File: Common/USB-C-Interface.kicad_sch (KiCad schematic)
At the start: 6 parts

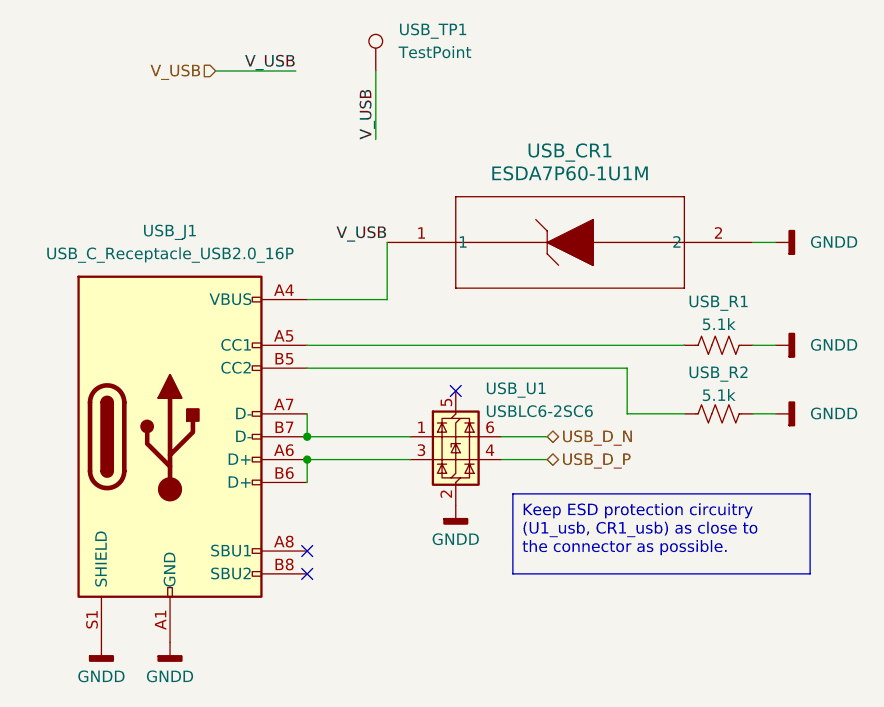
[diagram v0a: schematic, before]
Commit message: Renamed GPS Module PCB files to Radio Module
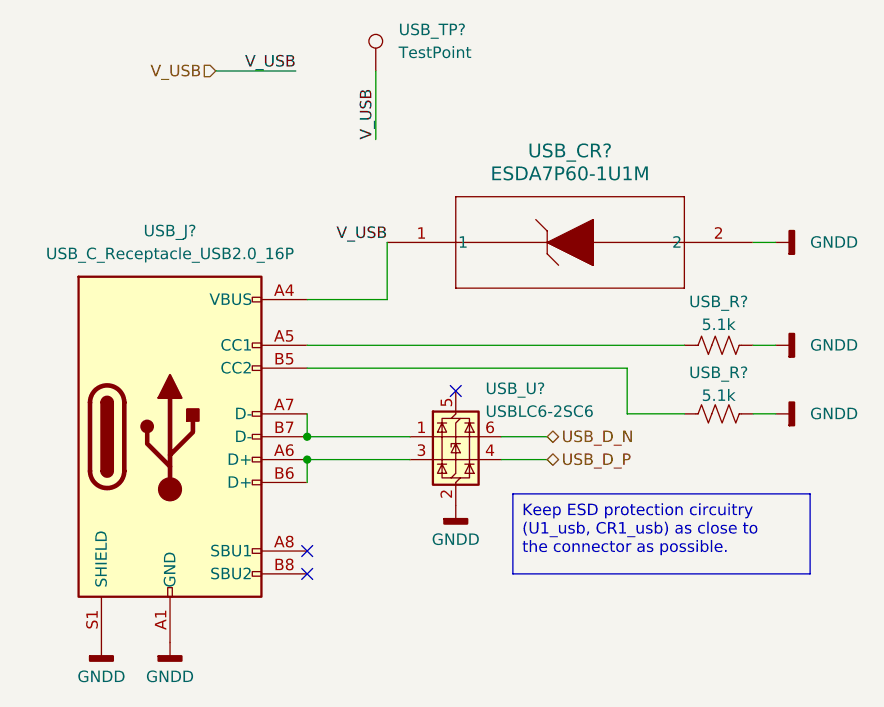
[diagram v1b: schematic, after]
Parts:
- renumbered USB_CR1 to USB_CR?, USB_J1 to USB_J?, USB_R2 to USB_R?, USB_R1 to USB_R?, USB_TP1 to USB_TP?, USB_U1 to USB_U?
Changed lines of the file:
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@@
 		(on_board yes)
 		(dnp no)
-		(property "Reference" "USB_U1"
+		(property "Reference" "USB_U?"
 			(at 82.042 72.136 0)
 			(effects
@@
 		)
 		(instances
+			(project "Radio-Module"
+				(path "/acc63f22-7eb8-450a-9af4-da5f4b8157d9/066db7ca-fd8b-46d1-a06b-412eb11482f3"
+					(reference "USB_U?")
+					(unit 1)
+				)
+			)
 			(project "Main-Module"
 				(path "/c41b490b-5ab6-4438-aea0-388670bb08f4/b23d16a1-3c5b-4321-8b30-5d6992e2f62d"
@@
 		(dnp no)
 		(fields_autoplaced yes)
-		(property "Reference" "USB_J1"
+		(property "Reference" "USB_J?"
 			(at 46.99 54.61 0)
 			(effects
@@
 		)
 		(instances
+			(project "Radio-Module"
+				(path "/acc63f22-7eb8-450a-9af4-da5f4b8157d9/066db7ca-fd8b-46d1-a06b-412eb11482f3"
+					(reference "USB_J?")
+					(unit 1)
+				)
+			)
 			(project "Main-Module"
 				(path "/c41b490b-5ab6-4438-aea0-388670bb08f4/b23d16a1-3c5b-4321-8b30-5d6992e2f62d"
@@
 		(dnp no)
 		(fields_autoplaced yes)
-		(property "Reference" "#PWR037"
+		(property "Reference" "#PWR?"
 			(at 46.99 106.68 0)
 			(effects
@@
 		)
 		(instances
+			(project "Radio-Module"
+				(path "/acc63f22-7eb8-450a-9af4-da5f4b8157d9/066db7ca-fd8b-46d1-a06b-412eb11482f3"
+					(reference "#PWR?")
+					(unit 1)
+				)
+			)
 			(project "Main-Module"
 				(path "/c41b490b-5ab6-4438-aea0-388670bb08f4/b23d16a1-3c5b-4321-8b30-5d6992e2f62d"
@@
 		(dnp no)
 		(fields_autoplaced yes)
-		(property "Reference" "#PWR039"
+		(property "Reference" "#PWR?"
 			(at 120.65 55.88 0)
 			(effects
@@
 		)
 		(instances
+			(project "Radio-Module"
+				(path "/acc63f22-7eb8-450a-9af4-da5f4b8157d9/066db7ca-fd8b-46d1-a06b-412eb11482f3"
+					(reference "#PWR?")
+					(unit 1)
+				)
+			)
 			(project "Main-Module"
 				(path "/c41b490b-5ab6-4438-aea0-388670bb08f4/b23d16a1-3c5b-4321-8b30-5d6992e2f62d"
@@
 		(dnp no)
 		(fields_autoplaced yes)
-		(property "Reference" "#PWR036"
+		(property "Reference" "#PWR?"
 			(at 39.37 106.68 0)
 			(effects
@@
 		)
 		(instances
+			(project "Radio-Module"
+				(path "/acc63f22-7eb8-450a-9af4-da5f4b8157d9/066db7ca-fd8b-46d1-a06b-412eb11482f3"
+					(reference "#PWR?")
+					(unit 1)
+				)
+			)
 			(project "Main-Module"
 				(path "/c41b490b-5ab6-4438-aea0-388670bb08f4/b23d16a1-3c5b-4321-8b30-5d6992e2f62d"
@@
 		(on_board yes)
 		(dnp no)
-		(property "Reference" "USB_R2"
+		(property "Reference" "USB_R?"
 			(at 107.95 70.358 90)
 			(effects
@@
 		)
 		(instances
+			(project "Radio-Module"
+				(path "/acc63f22-7eb8-450a-9af4-da5f4b8157d9/066db7ca-fd8b-46d1-a06b-412eb11482f3"
+					(reference "USB_R?")
+					(unit 1)
+				)
+			)
 			(project "Main-Module"
 				(path "/c41b490b-5ab6-4438-aea0-388670bb08f4/b23d16a1-3c5b-4321-8b30-5d6992e2f62d"
@@
 		(on_board yes)
 		(dnp no)
-		(property "Reference" "USB_R1"
+		(property "Reference" "USB_R?"
 			(at 107.95 62.484 90)
 			(effects
@@
 		)
 		(instances
+			(project "Radio-Module"
+				(path "/acc63f22-7eb8-450a-9af4-da5f4b8157d9/066db7ca-fd8b-46d1-a06b-412eb11482f3"
+					(reference "USB_R?")
+					(unit 1)
+				)
+			)
 			(project "Main-Module"
 				(path "/c41b490b-5ab6-4438-aea0-388670bb08f4/b23d16a1-3c5b-4321-8b30-5d6992e2f62d"
@@
 		(dnp no)
 		(fields_autoplaced yes)
-		(property "Reference" "USB_CR1"
+		(property "Reference" "USB_CR?"
 			(at 91.44 45.72 0)
 			(effects
@@
 		)
 		(instances
+			(project "Radio-Module"
+				(path "/acc63f22-7eb8-450a-9af4-da5f4b8157d9/066db7ca-fd8b-46d1-a06b-412eb11482f3"
+					(reference "USB_CR?")
+					(unit 1)
+				)
+			)
 			(project "Main-Module"
 				(path "/c41b490b-5ab6-4438-aea0-388670bb08f4/b23d16a1-3c5b-4321-8b30-5d6992e2f62d"
@@
 		(dnp no)
 		(fields_autoplaced yes)
-		(property "Reference" "#PWR041"
+		(property "Reference" "#PWR?"
 			(at 120.65 74.93 0)
 			(effects
@@
 		)
 		(instances
+			(project "Radio-Module"
+				(path "/acc63f22-7eb8-450a-9af4-da5f4b8157d9/066db7ca-fd8b-46d1-a06b-412eb11482f3"
+					(reference "#PWR?")
+					(unit 1)
+				)
+			)
 			(project "Main-Module"
 				(path "/c41b490b-5ab6-4438-aea0-388670bb08f4/b23d16a1-3c5b-4321-8b30-5d6992e2f62d"
@@
 		(dnp no)
 		(fields_autoplaced yes)
-		(property "Reference" "#PWR038"
+		(property "Reference" "#PWR?"
 			(at 78.74 91.44 0)
 			(effects
@@
 		)
 		(instances
+			(project "Radio-Module"
+				(path "/acc63f22-7eb8-450a-9af4-da5f4b8157d9/066db7ca-fd8b-46d1-a06b-412eb11482f3"
+					(reference "#PWR?")
+					(unit 1)
+				)
+			)
 			(project "Main-Module"
 				(path "/c41b490b-5ab6-4438-aea0-388670bb08f4/b23d16a1-3c5b-4321-8b30-5d6992e2f62d"
@@
 		(dnp no)
 		(fields_autoplaced yes)
-		(property "Reference" "#PWR040"
+		(property "Reference" "#PWR?"
 			(at 120.65 67.31 0)
 			(effects
@@
 		)
 		(instances
+			(project "Radio-Module"
+				(path "/acc63f22-7eb8-450a-9af4-da5f4b8157d9/066db7ca-fd8b-46d1-a06b-412eb11482f3"
+					(reference "#PWR?")
+					(unit 1)
+				)
+			)
 			(project "Main-Module"
 				(path "/c41b490b-5ab6-4438-aea0-388670bb08f4/b23d16a1-3c5b-4321-8b30-5d6992e2f62d"
@@
 		(dnp no)
 		(fields_autoplaced yes)
-		(property "Reference" "USB_TP1"
+		(property "Reference" "USB_TP?"
 			(at 72.39 32.2579 0)
 			(effects
@@
 		)
 		(instances
-			(project "Main-Module"
-				(path "/c41b490b-5ab6-4438-aea0-388670bb08f4/b23d16a1-3c5b-4321-8b30-5d6992e2f62d"
+			(project "Radio-Module"
+				(path "/acc63f22-7eb8-450a-9af4-da5f4b8157d9/066db7ca-fd8b-46d1-a06b-412eb11482f3"
+					(reference "USB_TP?")
+					(unit 1)
+				)
+			)
+			(project "Main-Module"
+				(path "/c41b490b-5ab6-4438-aea0-388670bb08f4/b23d16a1-3c5b-4321-8b30-5d6992e2f62d"

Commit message: Schematic for STM32U545RE
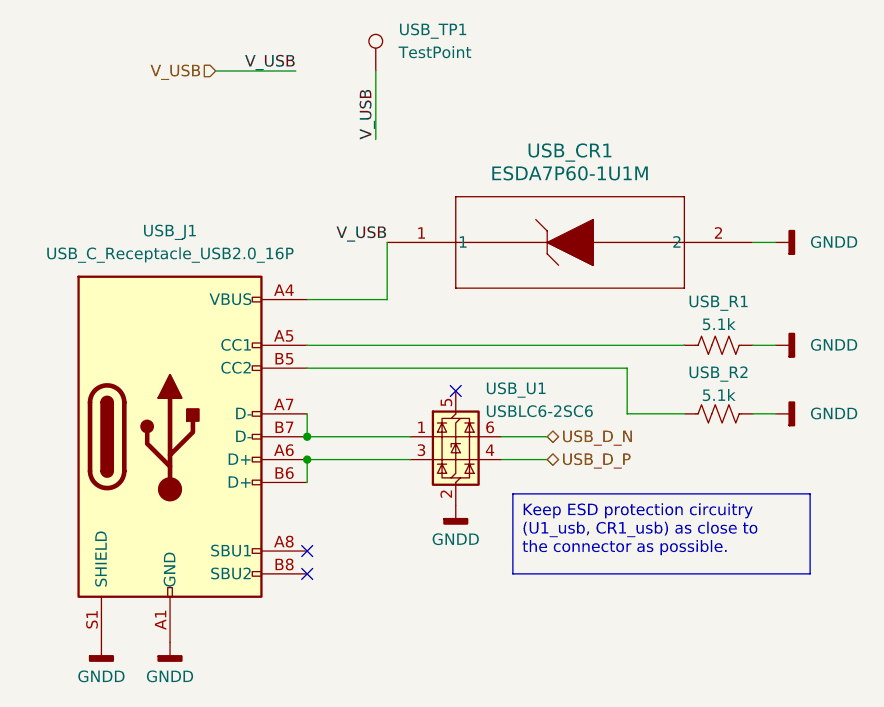
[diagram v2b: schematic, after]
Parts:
- gave numbers to parts that had none: 6
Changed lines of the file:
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@@
 		(on_board yes)
 		(dnp no)
-		(property "Reference" "USB_U?"
+		(property "Reference" "USB_U1"
 			(at 82.042 72.136 0)
 			(effects
@@
 		)
 		(instances
+			(project "USB-C-Interface"
+				(path "/7c253a73-a3ad-4431-8c8c-7421e0c0a047"
+					(reference "USB_U1")
+					(unit 1)
+				)
+			)
 			(project "Radio-Module"
 				(path "/acc63f22-7eb8-450a-9af4-da5f4b8157d9/066db7ca-fd8b-46d1-a06b-412eb11482f3"
@@
 		(dnp no)
 		(fields_autoplaced yes)
-		(property "Reference" "USB_J?"
+		(property "Reference" "USB_J1"
 			(at 46.99 54.61 0)
 			(effects
@@
 		)
 		(instances
+			(project "USB-C-Interface"
+				(path "/7c253a73-a3ad-4431-8c8c-7421e0c0a047"
+					(reference "USB_J1")
+					(unit 1)
+				)
+			)
 			(project "Radio-Module"
 				(path "/acc63f22-7eb8-450a-9af4-da5f4b8157d9/066db7ca-fd8b-46d1-a06b-412eb11482f3"
@@
 		(dnp no)
 		(fields_autoplaced yes)
-		(property "Reference" "#PWR?"
+		(property "Reference" "#PWR02"
 			(at 46.99 106.68 0)
 			(effects
@@
 		)
 		(instances
+			(project "USB-C-Interface"
+				(path "/7c253a73-a3ad-4431-8c8c-7421e0c0a047"
+					(reference "#PWR02")
+					(unit 1)
+				)
+			)
 			(project "Radio-Module"
 				(path "/acc63f22-7eb8-450a-9af4-da5f4b8157d9/066db7ca-fd8b-46d1-a06b-412eb11482f3"
@@
 		(dnp no)
 		(fields_autoplaced yes)
-		(property "Reference" "#PWR?"
+		(property "Reference" "#PWR04"
 			(at 120.65 55.88 0)
 			(effects
@@
 		)
 		(instances
+			(project "USB-C-Interface"
+				(path "/7c253a73-a3ad-4431-8c8c-7421e0c0a047"
+					(reference "#PWR04")
+					(unit 1)
+				)
+			)
 			(project "Radio-Module"
 				(path "/acc63f22-7eb8-450a-9af4-da5f4b8157d9/066db7ca-fd8b-46d1-a06b-412eb11482f3"
@@
 		(dnp no)
 		(fields_autoplaced yes)
-		(property "Reference" "#PWR?"
+		(property "Reference" "#PWR01"
 			(at 39.37 106.68 0)
 			(effects
@@
 		)
 		(instances
+			(project "USB-C-Interface"
+				(path "/7c253a73-a3ad-4431-8c8c-7421e0c0a047"
+					(reference "#PWR01")
+					(unit 1)
+				)
+			)
 			(project "Radio-Module"
 				(path "/acc63f22-7eb8-450a-9af4-da5f4b8157d9/066db7ca-fd8b-46d1-a06b-412eb11482f3"
@@
 		(on_board yes)
 		(dnp no)
-		(property "Reference" "USB_R?"
+		(property "Reference" "USB_R2"
 			(at 107.95 70.358 90)
 			(effects
@@
 		)
 		(instances
+			(project "USB-C-Interface"
+				(path "/7c253a73-a3ad-4431-8c8c-7421e0c0a047"
+					(reference "USB_R2")
+					(unit 1)
+				)
+			)
 			(project "Radio-Module"
 				(path "/acc63f22-7eb8-450a-9af4-da5f4b8157d9/066db7ca-fd8b-46d1-a06b-412eb11482f3"
@@
 		(on_board yes)
 		(dnp no)
-		(property "Reference" "USB_R?"
+		(property "Reference" "USB_R1"
 			(at 107.95 62.484 90)
 			(effects
@@
 		)
 		(instances
+			(project "USB-C-Interface"
+				(path "/7c253a73-a3ad-4431-8c8c-7421e0c0a047"
+					(reference "USB_R1")
+					(unit 1)
+				)
+			)
 			(project "Radio-Module"
 				(path "/acc63f22-7eb8-450a-9af4-da5f4b8157d9/066db7ca-fd8b-46d1-a06b-412eb11482f3"
@@
 		(dnp no)
 		(fields_autoplaced yes)
-		(property "Reference" "USB_CR?"
+		(property "Reference" "USB_CR1"
 			(at 91.44 45.72 0)
 			(effects
@@
 		)
 		(instances
+			(project "USB-C-Interface"
+				(path "/7c253a73-a3ad-4431-8c8c-7421e0c0a047"
+					(reference "USB_CR1")
+					(unit 1)
+				)
+			)
 			(project "Radio-Module"
 				(path "/acc63f22-7eb8-450a-9af4-da5f4b8157d9/066db7ca-fd8b-46d1-a06b-412eb11482f3"
@@
 		(dnp no)
 		(fields_autoplaced yes)
-		(property "Reference" "#PWR?"
+		(property "Reference" "#PWR06"
 			(at 120.65 74.93 0)
 			(effects
@@
 		)
 		(instances
+			(project "USB-C-Interface"
+				(path "/7c253a73-a3ad-4431-8c8c-7421e0c0a047"
+					(reference "#PWR06")
+					(unit 1)
+				)
+			)
 			(project "Radio-Module"
 				(path "/acc63f22-7eb8-450a-9af4-da5f4b8157d9/066db7ca-fd8b-46d1-a06b-412eb11482f3"
@@
 		(dnp no)
 		(fields_autoplaced yes)
-		(property "Reference" "#PWR?"
+		(property "Reference" "#PWR03"
 			(at 78.74 91.44 0)
 			(effects
@@
 		)
 		(instances
+			(project "USB-C-Interface"
+				(path "/7c253a73-a3ad-4431-8c8c-7421e0c0a047"
+					(reference "#PWR03")
+					(unit 1)
+				)
+			)
 			(project "Radio-Module"
 				(path "/acc63f22-7eb8-450a-9af4-da5f4b8157d9/066db7ca-fd8b-46d1-a06b-412eb11482f3"
@@
 		(dnp no)
 		(fields_autoplaced yes)
-		(property "Reference" "#PWR?"
+		(property "Reference" "#PWR05"
 			(at 120.65 67.31 0)
 			(effects
@@
 		)
 		(instances
+			(project "USB-C-Interface"
+				(path "/7c253a73-a3ad-4431-8c8c-7421e0c0a047"
+					(reference "#PWR05")
+					(unit 1)
+				)
+			)
 			(project "Radio-Module"
 				(path "/acc63f22-7eb8-450a-9af4-da5f4b8157d9/066db7ca-fd8b-46d1-a06b-412eb11482f3"
@@
 		(dnp no)
 		(fields_autoplaced yes)
-		(property "Reference" "USB_TP?"
+		(property "Reference" "USB_TP1"
 			(at 72.39 32.2579 0)
 			(effects
@@
 		)
 		(instances
+			(project "USB-C-Interface"
+				(path "/7c253a73-a3ad-4431-8c8c-7421e0c0a047"
+					(reference "USB_TP1")
+					(unit 1)
+				)
+			)
 			(project "Radio-Module"
 				(path "/acc63f22-7eb8-450a-9af4-da5f4b8157d9/066db7ca-fd8b-46d1-a06b-412eb11482f3"
@@
 		)
 	)
+	(sheet_instances
+		(path "/"
+			(page "1")
+		)
+	)

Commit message: Revert "Resolved recovery dev merge"
This reverts commit 81c4bbda93894cf9b120906f02d3dbab6bbd1e60, reversing
changes made to 220360569fc6c62025a0e7a68270d7f77f4a1f37.
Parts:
- renumbered USB_CR1 to USB_CR?, USB_J1 to USB_J?, USB_R2 to USB_R?, USB_R1 to USB_R?, USB_TP1 to USB_TP?, USB_U1 to USB_U?
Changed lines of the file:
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@@
 		(on_board yes)
 		(dnp no)
-		(property "Reference" "USB_U1"
+		(property "Reference" "USB_U?"
 			(at 82.042 72.136 0)
 			(effects
@@
 		)
 		(instances
-			(project "USB-C-Interface"
-				(path "/7c253a73-a3ad-4431-8c8c-7421e0c0a047"
-					(reference "USB_U1")
-					(unit 1)
-				)
-			)
 			(project "Radio-Module"
 				(path "/acc63f22-7eb8-450a-9af4-da5f4b8157d9/066db7ca-fd8b-46d1-a06b-412eb11482f3"
@@
 		(dnp no)
 		(fields_autoplaced yes)
-		(property "Reference" "USB_J1"
+		(property "Reference" "USB_J?"
 			(at 46.99 54.61 0)
 			(effects
@@
 		)
 		(instances
-			(project "USB-C-Interface"
-				(path "/7c253a73-a3ad-4431-8c8c-7421e0c0a047"
-					(reference "USB_J1")
-					(unit 1)
-				)
-			)
 			(project "Radio-Module"
 				(path "/acc63f22-7eb8-450a-9af4-da5f4b8157d9/066db7ca-fd8b-46d1-a06b-412eb11482f3"
@@
 		(dnp no)
 		(fields_autoplaced yes)
-		(property "Reference" "#PWR02"
+		(property "Reference" "#PWR?"
 			(at 46.99 106.68 0)
 			(effects
@@
 		)
 		(instances
-			(project "USB-C-Interface"
-				(path "/7c253a73-a3ad-4431-8c8c-7421e0c0a047"
-					(reference "#PWR02")
-					(unit 1)
-				)
-			)
 			(project "Radio-Module"
 				(path "/acc63f22-7eb8-450a-9af4-da5f4b8157d9/066db7ca-fd8b-46d1-a06b-412eb11482f3"
@@
 		(dnp no)
 		(fields_autoplaced yes)
-		(property "Reference" "#PWR04"
+		(property "Reference" "#PWR?"
 			(at 120.65 55.88 0)
 			(effects
@@
 		)
 		(instances
-			(project "USB-C-Interface"
-				(path "/7c253a73-a3ad-4431-8c8c-7421e0c0a047"
-					(reference "#PWR04")
-					(unit 1)
-				)
-			)
 			(project "Radio-Module"
 				(path "/acc63f22-7eb8-450a-9af4-da5f4b8157d9/066db7ca-fd8b-46d1-a06b-412eb11482f3"
@@
 		(dnp no)
 		(fields_autoplaced yes)
-		(property "Reference" "#PWR01"
+		(property "Reference" "#PWR?"
 			(at 39.37 106.68 0)
 			(effects
@@
 		)
 		(instances
-			(project "USB-C-Interface"
-				(path "/7c253a73-a3ad-4431-8c8c-7421e0c0a047"
-					(reference "#PWR01")
-					(unit 1)
-				)
-			)
 			(project "Radio-Module"
 				(path "/acc63f22-7eb8-450a-9af4-da5f4b8157d9/066db7ca-fd8b-46d1-a06b-412eb11482f3"
@@
 		(on_board yes)
 		(dnp no)
-		(property "Reference" "USB_R2"
+		(property "Reference" "USB_R?"
 			(at 107.95 70.358 90)
 			(effects
@@
 		)
 		(instances
-			(project "USB-C-Interface"
-				(path "/7c253a73-a3ad-4431-8c8c-7421e0c0a047"
-					(reference "USB_R2")
-					(unit 1)
-				)
-			)
 			(project "Radio-Module"
 				(path "/acc63f22-7eb8-450a-9af4-da5f4b8157d9/066db7ca-fd8b-46d1-a06b-412eb11482f3"
@@
 		(on_board yes)
 		(dnp no)
-		(property "Reference" "USB_R1"
+		(property "Reference" "USB_R?"
 			(at 107.95 62.484 90)
 			(effects
@@
 		)
 		(instances
-			(project "USB-C-Interface"
-				(path "/7c253a73-a3ad-4431-8c8c-7421e0c0a047"
-					(reference "USB_R1")
-					(unit 1)
-				)
-			)
 			(project "Radio-Module"
 				(path "/acc63f22-7eb8-450a-9af4-da5f4b8157d9/066db7ca-fd8b-46d1-a06b-412eb11482f3"
@@
 		(dnp no)
 		(fields_autoplaced yes)
-		(property "Reference" "USB_CR1"
+		(property "Reference" "USB_CR?"
 			(at 91.44 45.72 0)
 			(effects
@@
 		)
 		(instances
-			(project "USB-C-Interface"
-				(path "/7c253a73-a3ad-4431-8c8c-7421e0c0a047"
-					(reference "USB_CR1")
-					(unit 1)
-				)
-			)
 			(project "Radio-Module"
 				(path "/acc63f22-7eb8-450a-9af4-da5f4b8157d9/066db7ca-fd8b-46d1-a06b-412eb11482f3"
@@
 		(dnp no)
 		(fields_autoplaced yes)
-		(property "Reference" "#PWR06"
+		(property "Reference" "#PWR?"
 			(at 120.65 74.93 0)
 			(effects
@@
 		)
 		(instances
-			(project "USB-C-Interface"
-				(path "/7c253a73-a3ad-4431-8c8c-7421e0c0a047"
-					(reference "#PWR06")
-					(unit 1)
-				)
-			)
 			(project "Radio-Module"
 				(path "/acc63f22-7eb8-450a-9af4-da5f4b8157d9/066db7ca-fd8b-46d1-a06b-412eb11482f3"
@@
 		(dnp no)
 		(fields_autoplaced yes)
-		(property "Reference" "#PWR03"
+		(property "Reference" "#PWR?"
 			(at 78.74 91.44 0)
 			(effects
@@
 		)
 		(instances
-			(project "USB-C-Interface"
-				(path "/7c253a73-a3ad-4431-8c8c-7421e0c0a047"
-					(reference "#PWR03")
-					(unit 1)
-				)
-			)
 			(project "Radio-Module"
 				(path "/acc63f22-7eb8-450a-9af4-da5f4b8157d9/066db7ca-fd8b-46d1-a06b-412eb11482f3"
@@
 		(dnp no)
 		(fields_autoplaced yes)
-		(property "Reference" "#PWR05"
+		(property "Reference" "#PWR?"
 			(at 120.65 67.31 0)
 			(effects
@@
 		)
 		(instances
-			(project "USB-C-Interface"
-				(path "/7c253a73-a3ad-4431-8c8c-7421e0c0a047"
-					(reference "#PWR05")
-					(unit 1)
-				)
-			)
 			(project "Radio-Module"
 				(path "/acc63f22-7eb8-450a-9af4-da5f4b8157d9/066db7ca-fd8b-46d1-a06b-412eb11482f3"
@@
 		(dnp no)
 		(fields_autoplaced yes)
-		(property "Reference" "USB_TP1"
+		(property "Reference" "USB_TP?"
 			(at 72.39 32.2579 0)
 			(effects
@@
 		)
 		(instances
-			(project "USB-C-Interface"
-				(path "/7c253a73-a3ad-4431-8c8c-7421e0c0a047"
+			(project "Radio-Module"
+				(path "/acc63f22-7eb8-450a-9af4-da5f4b8157d9/066db7ca-fd8b-46d1-a06b-412eb11482f3"
+					(reference "USB_TP?")
+					(unit 1)
+				)
+			)
+			(project "Main-Module"
+				(path "/c41b490b-5ab6-4438-aea0-388670bb08f4/b23d16a1-3c5b-4321-8b30-5d6992e2f62d"
 					(reference "USB_TP1")
 					(unit 1)
 				)
 			)
-			(project "Radio-Module"
-				(path "/acc63f22-7eb8-450a-9af4-da5f4b8157d9/066db7ca-fd8b-46d1-a06b-412eb11482f3"
-					(reference "USB_TP?")
-					(unit 1)
-				)
-			)
-			(project "Main-Module"
-				(path "/c41b490b-5ab6-4438-aea0-388670bb08f4/b23d16a1-3c5b-4321-8b30-5d6992e2f62d"
-					(reference "USB_TP1")
-					(unit 1)
-				)
-			)
-		)
-	)
-	(sheet_instances
-		(path "/"
-			(page "1")
-		)
-	)
+		)
+	)
